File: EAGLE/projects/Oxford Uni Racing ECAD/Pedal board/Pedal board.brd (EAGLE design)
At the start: 165.1 x 216.8 mm, 47 parts, among them J1 T821108A1S100CEU, J2 T821108A1S100CEU, J3 T821108A1S100CEU, J4 T821108A1S100CEU, J6 T821108A1S100CEU, J7 T821108A1S100CEU, K1 RT444012, T1 BT169, X2 D-SUB9-H2M09ST

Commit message: updated connector names on pedal board
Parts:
- J2: value T821108A1S100CEU -> THR_1_2
- J3: value T821108A1S100CEU -> PWR_CAN
- J4: value T821108A1S100CEU -> THR_3
- J6: value T821108A1S100CEU -> BR_POS_PRESS_STWH
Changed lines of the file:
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@@
 <attribute name="VALUE" x="82.9056" y="29.6926" size="0.9906" layer="27" ratio="12" rot="R180"/>
 </element>
-<element name="J3" library="T821108A1S100CEU" package="HDRV8W64P254_2X4_1778X895X915P" value="T821108A1S100CEU" x="90.17" y="22.86" smashed="yes" rot="R180">
+<element name="J3" library="T821108A1S100CEU" package="HDRV8W64P254_2X4_1778X895X915P" value="PWR_CAN" x="90.17" y="22.86" smashed="yes" rot="R180">
 <attribute name="DESCRIPTION" value="HEADER, VERTICAL, 2.54MM, 8WAY Amphenol T821 Series, 2.54mm Pitch 8 Way 2 Row Straight PCB Header, Solder Termination, 3A" x="93.98" y="22.86" size="1.778" layer="27" rot="R180" display="off"/>
 <attribute name="HEIGHT" value="9.15mm" x="93.98" y="22.86" size="1.778" layer="27" rot="R180" display="off"/>
@@
 <attribute name="VALUE" x="138.049" y="18.034" size="1.27" layer="27" ratio="10" rot="R180"/>
 </element>
-<element name="J2" library="T821108A1S100CEU" package="HDRV8W64P254_2X4_1778X895X915P" value="T821108A1S100CEU" x="147.32" y="34.29" smashed="yes">
+<element name="J2" library="T821108A1S100CEU" package="HDRV8W64P254_2X4_1778X895X915P" value="THR_1_2" x="147.32" y="34.29" smashed="yes">
 <attribute name="DESCRIPTION" value="HEADER, VERTICAL, 2.54MM, 8WAY Amphenol T821 Series, 2.54mm Pitch 8 Way 2 Row Straight PCB Header, Solder Termination, 3A" x="143.51" y="34.29" size="1.778" layer="27" display="off"/>
 <attribute name="HEIGHT" value="9.15mm" x="143.51" y="34.29" size="1.778" layer="27" display="off"/>
@@
 <attribute name="VALUE" x="149.86" y="31.75" size="1.27" layer="27" align="center"/>
 </element>
-<element name="J4" library="T821108A1S100CEU" package="HDRV8W64P254_2X4_1778X895X915P" value="T821108A1S100CEU" x="147.32" y="45.72" smashed="yes">
+<element name="J4" library="T821108A1S100CEU" package="HDRV8W64P254_2X4_1778X895X915P" value="THR_3" x="147.32" y="45.72" smashed="yes">
 <attribute name="DESCRIPTION" value="HEADER, VERTICAL, 2.54MM, 8WAY Amphenol T821 Series, 2.54mm Pitch 8 Way 2 Row Straight PCB Header, Solder Termination, 3A" x="144.78" y="45.72" size="1.778" layer="27" display="off"/>
 <attribute name="HEIGHT" value="9.15mm" x="144.78" y="45.72" size="1.778" layer="27" display="off"/>
@@
 <attribute name="VALUE" x="149.86" y="43.18" size="1.27" layer="27" align="center"/>
 </element>
-<element name="J6" library="T821108A1S100CEU" package="HDRV8W64P254_2X4_1778X895X915P" value="T821108A1S100CEU" x="8.89" y="-120.65" smashed="yes">
+<element name="J6" library="T821108A1S100CEU" package="HDRV8W64P254_2X4_1778X895X915P" value="BR_POS_PRESS_STWH" x="8.89" y="-120.65" smashed="yes">
 <attribute name="DESCRIPTION" value="HEADER, VERTICAL, 2.54MM, 8WAY Amphenol T821 Series, 2.54mm Pitch 8 Way 2 Row Straight PCB Header, Solder Termination, 3A" x="6.35" y="-120.65" size="1.778" layer="27" display="off"/>
 <attribute name="HEIGHT" value="9.15mm" x="6.35" y="-120.65" size="1.778" layer="27" display="off"/>

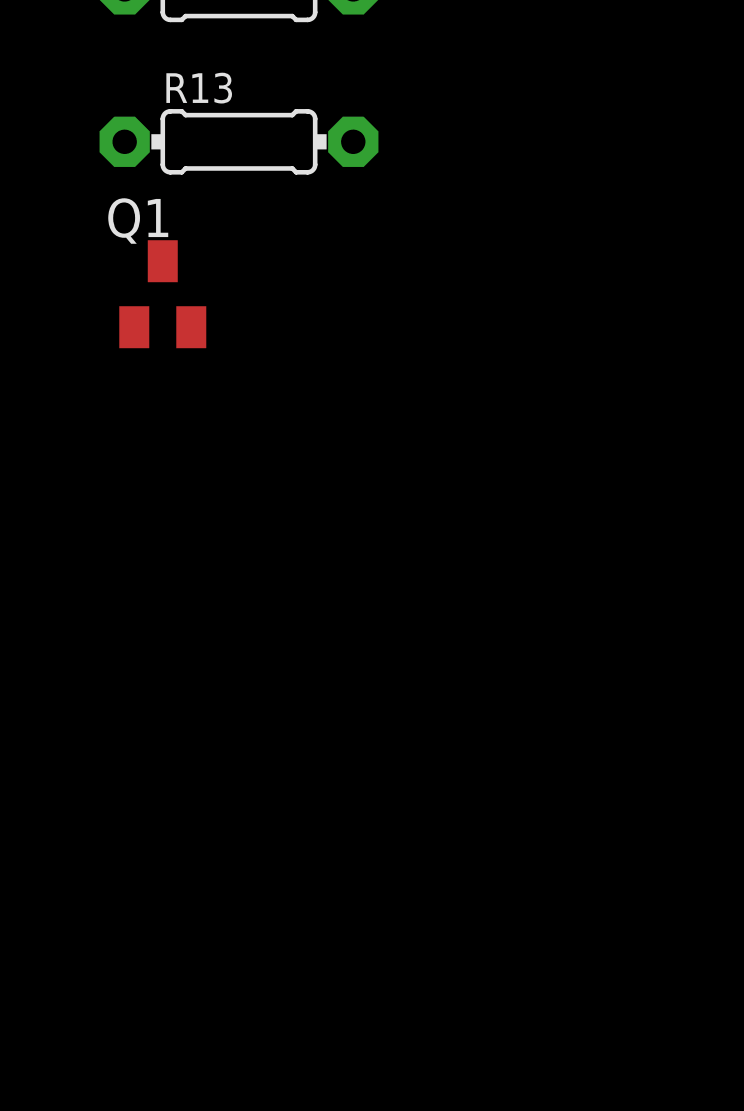
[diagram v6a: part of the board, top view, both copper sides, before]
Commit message: added op amp to fix voltage of brake pressure sensor
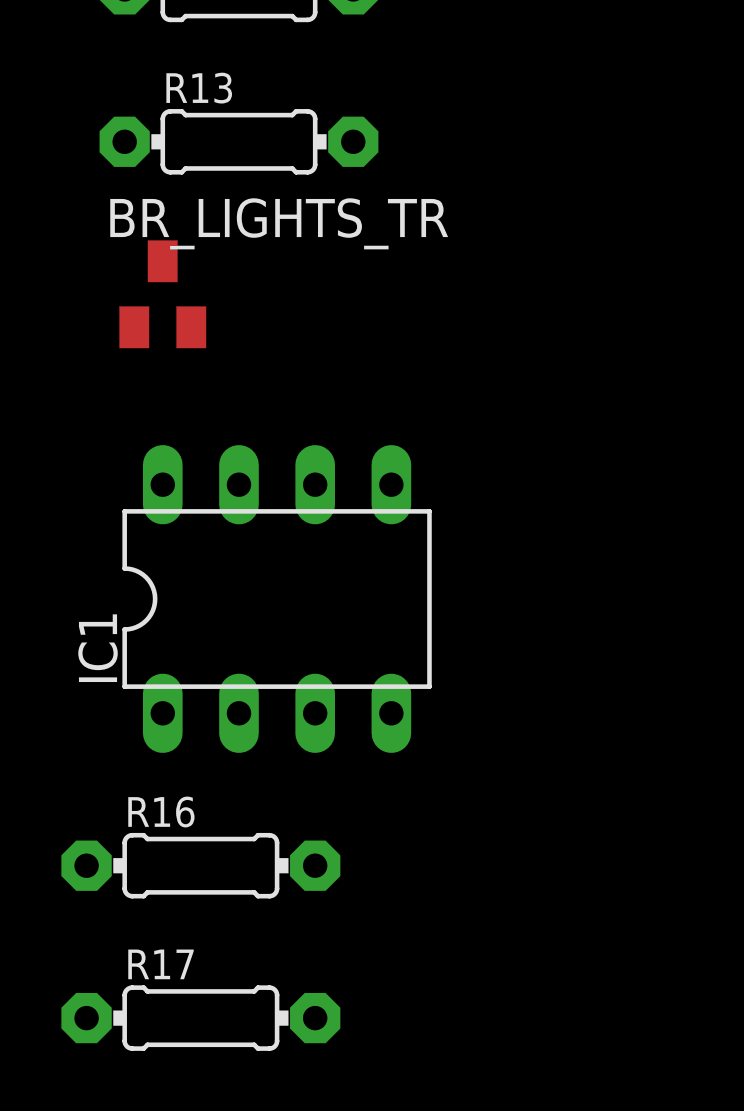
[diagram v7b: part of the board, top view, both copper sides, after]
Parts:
- added IC1: AD711N, analog-devices:DIL08
- added R16: 240, adafruit:0204/7
- added R17: 1K, adafruit:0204/7
- BR_LIGHTS_TR: value (none) -> IRLML2502GTRPBF
- renumbered Q1 to BR_LIGHTS_TR
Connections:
- new net N$23: IC1.2, IC1.6, R16.2
- new net N$27: IC1.3, J6.6
- net 12V: now also IC1.7
- net BR_PRESS: now also R16.1, R17.2; no longer J6.6
- net GND: now also IC1.4, R17.1
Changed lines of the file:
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@@
 <attribute name="VALUE" x="3.4544" y="-152.8826" size="0.9906" layer="27" ratio="12"/>
 </element>
-<element name="Q1" library="adafruit" library_urn="urn:adsk.eagle:library:420" package="SOT23" package3d_urn="urn:adsk.eagle:package:6240836/1" value="" x="2.54" y="-157.48" smashed="yes">
+<element name="BR_LIGHTS_TR" library="adafruit" library_urn="urn:adsk.eagle:library:420" package="SOT23" package3d_urn="urn:adsk.eagle:package:6240836/1" value="IRLML2502GTRPBF" x="2.54" y="-157.48" smashed="yes">
 <attribute name="NAME" x="0.635" y="-155.575" size="1.27" layer="25"/>
 <attribute name="VALUE" x="0.635" y="-160.655" size="1.27" layer="27"/>
+</element>
+<element name="IC1" library="analog-devices" library_urn="urn:adsk.eagle:library:102" package="DIL08" package3d_urn="urn:adsk.eagle:package:3915/1" value="AD711N" x="6.35" y="-167.64" smashed="yes">
+<attribute name="MF" value="" x="6.35" y="-167.64" size="1.778" layer="27" display="off"/>
+<attribute name="MPN" value="AD711BQ" x="6.35" y="-167.64" size="1.778" layer="27" display="off"/>
+<attribute name="NAME" x="1.016" y="-170.561" size="1.27" layer="25" ratio="10" rot="R90"/>
+<attribute name="OC_FARNELL" value="9604839" x="6.35" y="-167.64" size="1.778" layer="27" display="off"/>
+<attribute name="OC_NEWARK" value="66F5826" x="6.35" y="-167.64" size="1.778" layer="27" display="off"/>
+<attribute name="VALUE" x="2.794" y="-168.275" size="1.27" layer="27" ratio="10"/>
+</element>
+<element name="R16" library="adafruit" library_urn="urn:adsk.eagle:library:420" package="0204/7" package3d_urn="urn:adsk.eagle:package:6240596/1" value="240" x="3.81" y="-176.53" smashed="yes">
+<attribute name="NAME" x="1.27" y="-175.2346" size="0.9906" layer="25" ratio="12"/>
+<attribute name="VALUE" x="2.1844" y="-177.0126" size="0.9906" layer="27" ratio="12"/>
+</element>
+<element name="R17" library="adafruit" library_urn="urn:adsk.eagle:library:420" package="0204/7" package3d_urn="urn:adsk.eagle:package:6240596/1" value="1K" x="3.81" y="-181.61" smashed="yes">
+<attribute name="NAME" x="1.27" y="-180.3146" size="0.9906" layer="25" ratio="12"/>
+<attribute name="VALUE" x="2.1844" y="-182.0926" size="0.9906" layer="27" ratio="12"/>
 </element>
 </elements>
@@
 <contactref element="J6" pad="3"/>
 <contactref element="R13" pad="1"/>
-<contactref element="Q1" pad="2"/>
+<contactref element="BR_LIGHTS_TR" pad="2"/>
+<contactref element="IC1" pad="4"/>
+<contactref element="R17" pad="1"/>
 <wire x1="149.86" y1="36.83" x2="149.86" y2="45.72" width="0" layer="19" extent="1-1"/>
 <wire x1="149.86" y1="34.29" x2="149.86" y2="36.83" width="0" layer="19" extent="1-1"/>
@@
 <wire x1="1.27" y1="-152.4" x2="11.43" y2="-120.65" width="0" layer="19" extent="1-1"/>
 <wire x1="3.49" y1="-158.58" x2="1.27" y2="-152.4" width="0" layer="19" extent="1-1"/>
+<wire x1="10.16" y1="-171.45" x2="3.49" y2="-158.58" width="0" layer="19" extent="1-1"/>
+<wire x1="0" y1="-181.61" x2="10.16" y2="-171.45" width="0" layer="19" extent="1-1"/>
 </signal>
 <signal name="N$3">
@@
 <wire x1="129.54" y1="7.62" x2="125.73" y2="7.62" width="1.27" layer="16"/>
 <contactref element="J7" pad="8"/>
-<wire x1="111.76" y1="7.62" x2="125.73" y2="7.62" width="0" layer="19" extent="16-16"/>
+<contactref element="IC1" pad="7"/>
+<wire x1="16.51" y1="-138.43" x2="5.08" y2="-163.83" width="0" layer="19" extent="1-1"/>
+<wire x1="8.8866375" y1="-98.7666375" x2="16.51" y2="-138.43" width="0" layer="19" extent="16-16"/>
+<wire x1="23.8506" y1="-31.0388" x2="11.376653125" y2="-63.733675" width="0" layer="19" extent="16-16"/>
+<wire x1="102.87" y1="7.62" x2="71.11193125" y2="-68.1202625" width="0" layer="19" extent="16-16"/>
+<wire x1="125.73" y1="7.62" x2="111.76" y2="7.62" width="0" layer="19" extent="16-16"/>
 <wire x1="90.17" y1="20.32" x2="102.87" y2="7.62" width="0" layer="19" extent="16-16"/>
-<wire x1="71.11193125" y1="-68.1202625" x2="102.87" y2="7.62" width="0" layer="19" extent="16-16"/>
-<wire x1="23.8506" y1="-31.0388" x2="11.376653125" y2="-63.733675" width="0" layer="19" extent="16-16"/>
-<wire x1="16.51" y1="-138.43" x2="8.8866375" y2="-98.7666375" width="0" layer="19" extent="16-16"/>
 </signal>
 <signal name="CANL">
@@
 <contactref element="J6" pad="5"/>
 </signal>
-<signal name="BR_PRESS">
-<contactref element="J6" pad="6"/>
-</signal>
 <signal name="ST_WH_POSS">
 <contactref element="J6" pad="7"/>
@@
 <contactref element="R12" pad="2"/>
 <contactref element="R13" pad="2"/>
-<contactref element="Q1" pad="1"/>
+<contactref element="BR_LIGHTS_TR" pad="1"/>
 <wire x1="8.89" y1="-152.4" x2="1.59" y2="-158.58" width="0" layer="19" extent="1-1"/>
 <wire x1="8.89" y1="-147.32" x2="8.89" y2="-152.4" width="0" layer="19" extent="1-1"/>
@@
 <signal name="N$28">
 <contactref element="J7" pad="3"/>
-<contactref element="Q1" pad="3"/>
+<contactref element="BR_LIGHTS_TR" pad="3"/>
 <wire x1="11.43" y1="-140.97" x2="2.54" y2="-156.38" width="0" layer="19" extent="1-1"/>
 </signal>
+<signal name="N$23">
+<contactref element="IC1" pad="6"/>
+<contactref element="IC1" pad="2"/>
+<contactref element="R16" pad="2"/>
+<wire x1="5.08" y1="-171.45" x2="7.62" y2="-176.53" width="0" layer="19" extent="1-1"/>
+<wire x1="7.62" y1="-163.83" x2="5.08" y2="-171.45" width="0" layer="19" extent="1-1"/>
+</signal>
+<signal name="N$27">
+<contactref element="J6" pad="6"/>
+<contactref element="IC1" pad="3"/>
+<wire x1="13.97" y1="-118.11" x2="7.62" y2="-171.45" width="0" layer="19" extent="1-1"/>
+</signal>
+<signal name="BR_PRESS">
+<contactref element="R16" pad="1"/>
+<contactref element="R17" pad="2"/>
+<wire x1="7.62" y1="-181.61" x2="0" y2="-176.53" width="0" layer="19" extent="1-1"/>
+</signal>
 </signals>

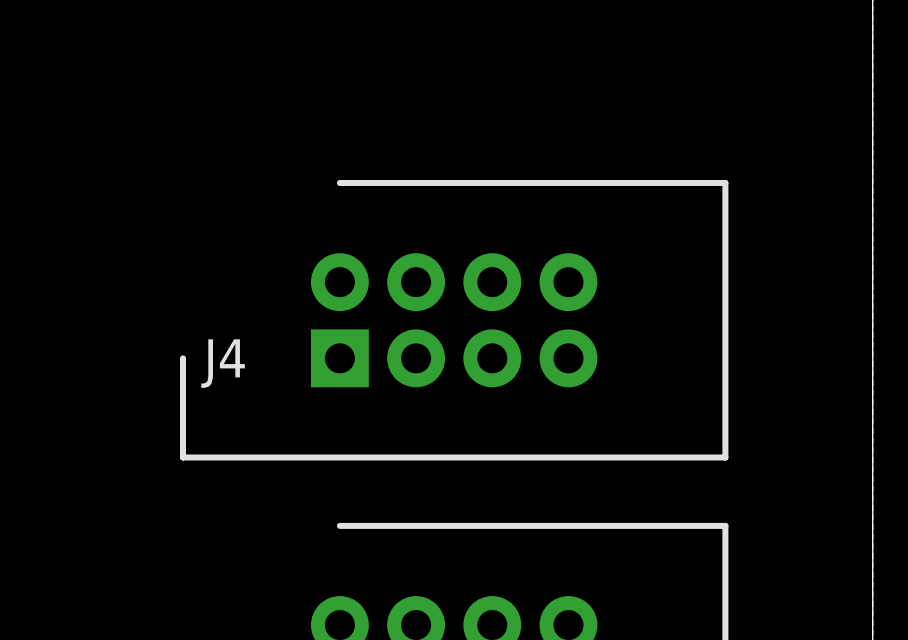
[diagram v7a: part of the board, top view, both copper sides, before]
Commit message: removed throttle position sensor 3 from all chematics
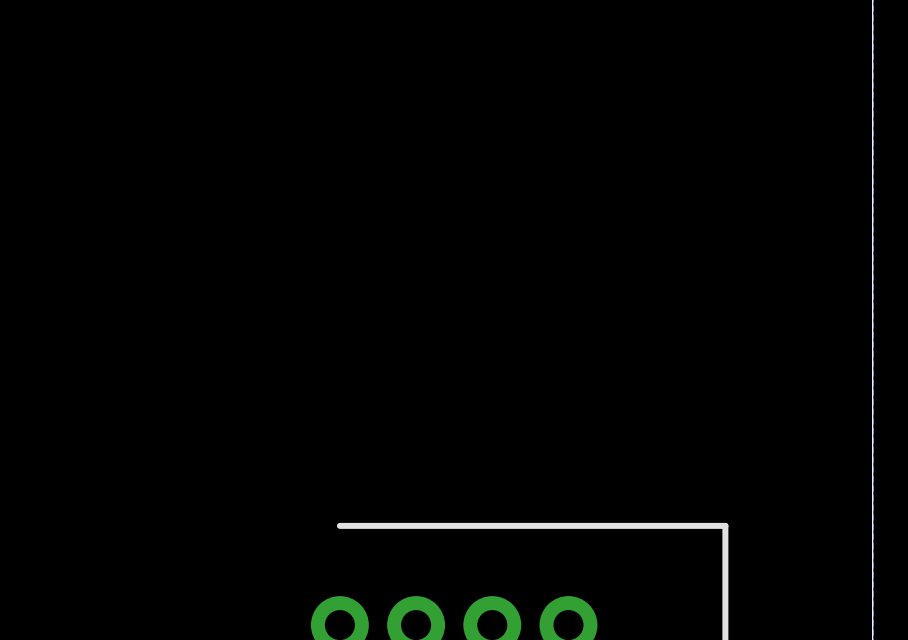
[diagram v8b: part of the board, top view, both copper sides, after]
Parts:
- removed J4: THR_3, T821108A1S100CEU:HDRV8W64P254_2X4_1778X895X915P
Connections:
- removed net THR3: J4.5
- net 3.3V: no longer J4.1
- net GND: no longer J4.3
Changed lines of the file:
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@@
 <attribute name="VALUE" x="149.86" y="31.75" size="1.27" layer="27" align="center"/>
-</element>
-<element name="J4" library="T821108A1S100CEU" package="HDRV8W64P254_2X4_1778X895X915P" value="THR_3" x="147.32" y="45.72" smashed="yes">
-<attribute name="DESCRIPTION" value="HEADER, VERTICAL, 2.54MM, 8WAY Amphenol T821 Series, 2.54mm Pitch 8 Way 2 Row Straight PCB Header, Solder Termination, 3A" x="144.78" y="45.72" size="1.778" layer="27" display="off"/>
-<attribute name="HEIGHT" value="9.15mm" x="144.78" y="45.72" size="1.778" layer="27" display="off"/>
-<attribute name="MANUFACTURER_NAME" value="Amphenol" x="144.78" y="45.72" size="1.778" layer="27" display="off"/>
-<attribute name="MANUFACTURER_PART_NUMBER" value="T821108A1S100CEU" x="144.78" y="45.72" size="1.778" layer="27" display="off"/>
-<attribute name="NAME" x="143.51" y="45.72" size="1.27" layer="25" align="center"/>
-<attribute name="RS_PART_NUMBER" value="1702738" x="144.78" y="45.72" size="1.778" layer="27" display="off"/>
-<attribute name="VALUE" x="149.86" y="43.18" size="1.27" layer="27" align="center"/>
 </element>
 <element name="J6" library="T821108A1S100CEU" package="HDRV8W64P254_2X4_1778X895X915P" value="BR_POS_PRESS_STWH" x="8.89" y="-120.65" smashed="yes">
@@
 <contactref element="J2" pad="3"/>
 <contactref element="J2" pad="4"/>
-<contactref element="J4" pad="3"/>
 <contactref element="J6" pad="3"/>
 <contactref element="R13" pad="1"/>
@@
 <contactref element="IC1" pad="4"/>
 <contactref element="R17" pad="1"/>
-<wire x1="149.86" y1="36.83" x2="149.86" y2="45.72" width="0" layer="19" extent="1-1"/>
 <wire x1="149.86" y1="34.29" x2="149.86" y2="36.83" width="0" layer="19" extent="1-1"/>
 <wire x1="134.62" y1="22.86" x2="149.86" y2="34.29" width="0" layer="19" extent="16-16"/>
@@
 <contactref element="J2" pad="6"/>
 </signal>
-<signal name="THR3">
-<contactref element="J4" pad="5"/>
-</signal>
 <signal name="3.3V">
 <contactref element="J2" pad="1"/>
 <contactref element="J2" pad="2"/>
-<contactref element="J4" pad="1"/>
 <contactref element="IC2" pad="2"/>
 <contactref element="C5" pad="1"/>
@@
 <wire x1="116.84" y1="21.59" x2="114.3" y2="21.59" width="1.27" layer="16"/>
 <contactref element="J6" pad="1"/>
-<wire x1="147.32" y1="36.83" x2="147.32" y2="45.72" width="0" layer="19" extent="1-1"/>
 <wire x1="147.32" y1="34.29" x2="147.32" y2="36.83" width="0" layer="19" extent="1-1"/>
 <wire x1="116.84" y1="21.59" x2="147.32" y2="34.29" width="0" layer="19" extent="1-1"/>
